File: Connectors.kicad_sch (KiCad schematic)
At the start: 10 parts, among them J14 200528-0100, J15 200528-0100, J16 200528-0100, J17 1824543, J18 200528-0100, J19 200528-0100, J2 200528-0100, J4 200528-0100, J6 200528-0100, J9 200528-0100

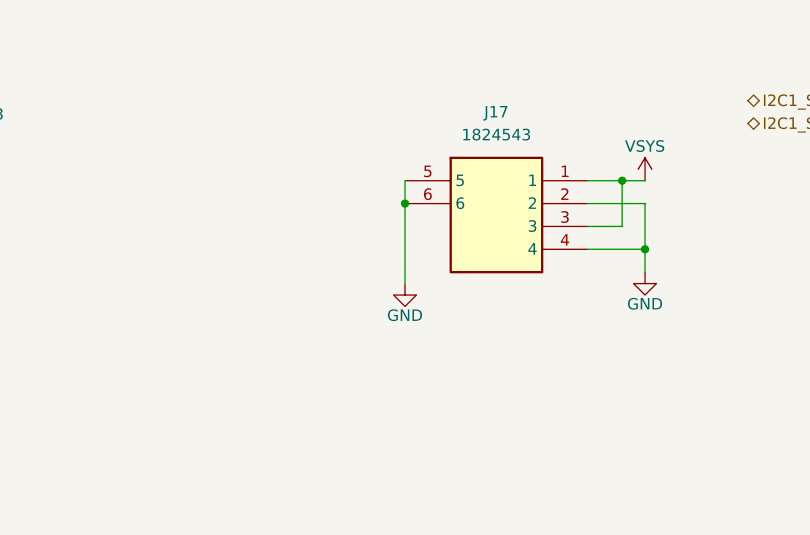
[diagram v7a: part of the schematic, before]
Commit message: Added better protection to SD card, Jetson IO, and added address breakouts to power monitors
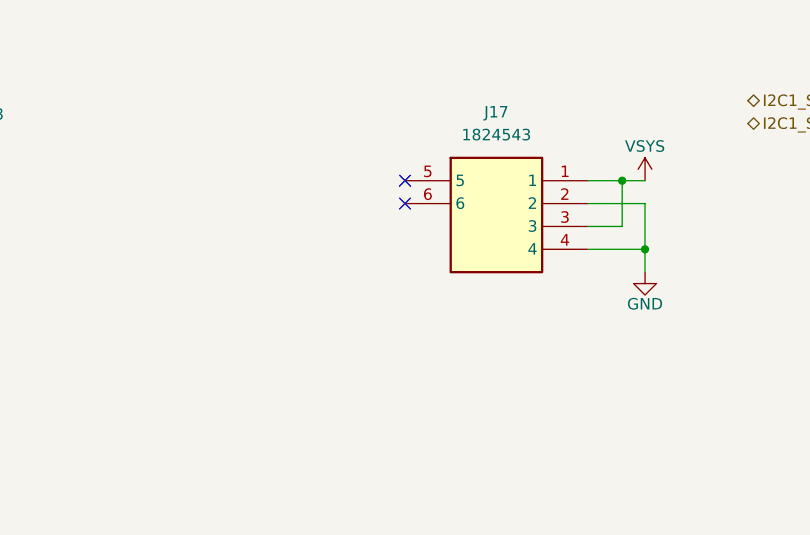
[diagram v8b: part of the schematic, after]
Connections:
- net GND: no longer J17.5, J17.6
- no-connect marks 0 -> 2
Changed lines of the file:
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@@
 	)
 	(junction
-		(at 173.99 39.37)
-		(diameter 0)
-		(color 0 0 0 0)
-	)
-	(junction
 		(at 127 41.91)
 		(diameter 0)
@@
 		(color 0 0 0 0)
 	)
+	(no_connect
+		(at 173.99 39.37)
+	)
+	(no_connect
+		(at 173.99 36.83)
+	)
 	(wire
 		(pts
@@
 	(wire
 		(pts
-			(xy 173.99 39.37) (xy 173.99 48.26)
-		)
-		(stroke
-			(width 0)
-			(type default)
-		)
-	)
-	(wire
-		(pts
 			(xy 41.91 118.11) (xy 36.83 118.11)
 		)
@@
 	(wire
 		(pts
-			(xy 173.99 36.83) (xy 173.99 39.37)
-		)
-		(stroke
-			(width 0)
-			(type default)
-		)
-	)
-	(wire
-		(pts
 			(xy 152.4 110.49) (xy 152.4 113.03)
 		)
@@
 					(unit 1)
 				)
-			)
-		)
-	)
-	(symbol
-		(lib_id "power:GND")
-		(at 173.99 48.26 0)
-		(unit 1)
-		(exclude_from_sim no)
-		(in_bom yes)
-		(on_board yes)
-		(dnp no)
-		(property "Reference" "#PWR0173"
-			(at 173.99 54.61 0)
-			(effects
-				(font
-					(size 1.27 1.27)
-				)
-				(hide yes)
-			)
-		)
-		(property "Value" "GND"
-			(at 173.99 51.816 0)
-			(effects
-				(font
-					(size 1.27 1.27)
-				)
-			)
-		)
-		(property "Footprint" ""
-			(at 173.99 48.26 0)
-			(effects
-				(font
-					(size 1.27 1.27)
-				)
-				(hide yes)
-			)
-		)
-		(property "Datasheet" ""
-			(at 173.99 48.26 0)
-			(effects
-				(font
-					(size 1.27 1.27)
-				)
-				(hide yes)
-			)
-		)
-		(property "Description" "Power symbol creates a global label with name \"GND\" , ground"
-			(at 173.99 48.26 0)
-			(effects
-				(font
-					(size 1.27 1.27)
-				)
-				(hide yes)
-			)
-		)
-		(pin "1"
-		)
-		(instances
-			(project "Avionics-MainBoard"
-				(path "/4c932743-8c6f-426e-9c1f-5a3f2b32c70d/4f4b7284-37b0-4a6d-8b77-acbb922141bd"
-					(reference "#PWR0173")
-					(unit 1)
-				)
